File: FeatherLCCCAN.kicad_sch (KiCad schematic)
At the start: 1 part

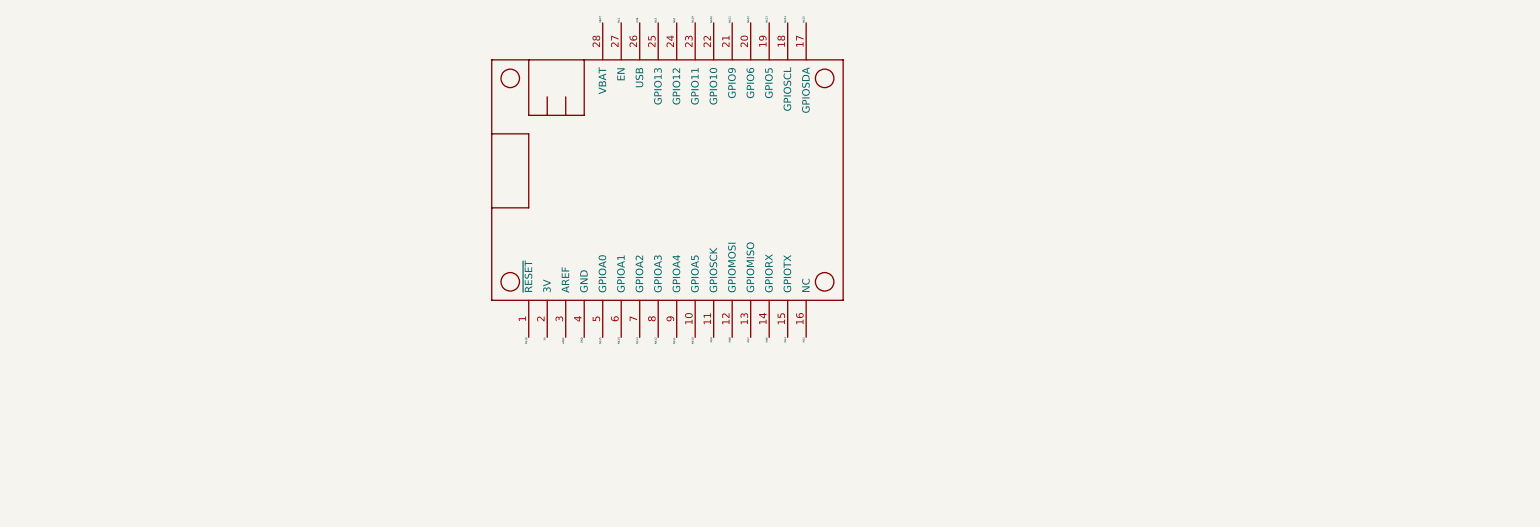
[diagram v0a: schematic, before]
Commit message: Completed LCC CAN Feather Wing.
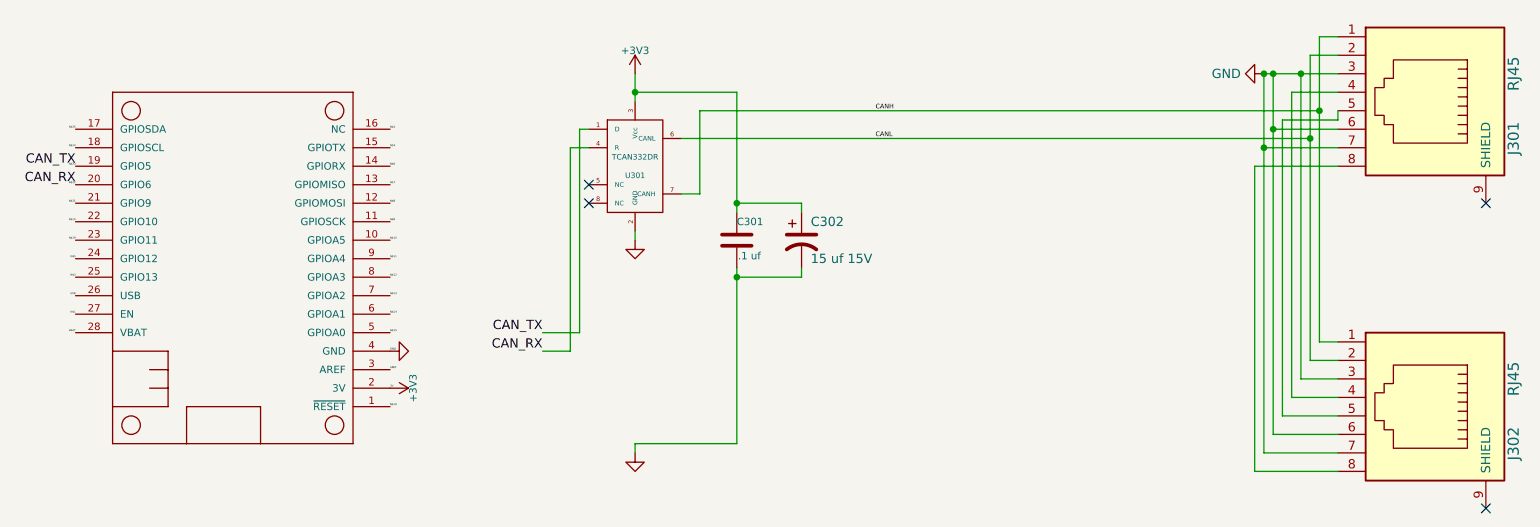
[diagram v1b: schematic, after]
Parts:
- added C301: .1 uf, Capacitor_SMD:C_0603_1608Metric, symbol ESP32-Mini32-OctalBuffer-rescue:C
- added C302: 15 uf 15V, Capacitor_SMD:CP_Elec_4x5.7, symbol ESP32-Mini32-OctalBuffer-rescue:CP1
- added J301, J302: RJ45, RJ45:RJ45_8N-S, symbol ESP32-Mini32-OctalBuffer-rescue:RJ45
- added U301: TCAN332DR, Package_SO:SOIC-8_3.9x4.9mm_P1.27mm, symbol sn65hvd233-ht:TCAN332DR
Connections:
- net GND: now also C301.2, C302.2, J301.3, J301.6, J301.7, J302.3, J302.6, J302.7, U301.2 (GND)
- net 3V renamed +3V3
- net +3V3: now also C301.1, C302.1, U301.3 (Vcc)
- net N$22 renamed CAN_RX
- net CAN_RX: now also U301.4 (R)
- net N$23 renamed CAN_TX
- net CAN_TX: now also U301.1 (D)
- new net: J301.4, J302.4
- new net: J301.5, J302.5
- new net: J301.8, J302.8
- new net CANH: J301.1, J302.1, U301.7 (CANH)
- new net CANL: J301.2, J302.2, U301.6 (CANL)
- no-connect marks 0 -> 4

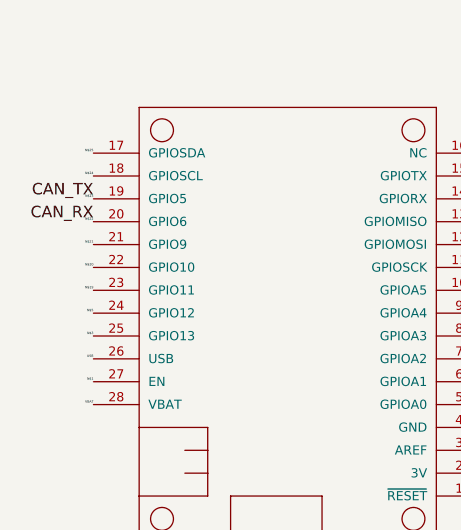
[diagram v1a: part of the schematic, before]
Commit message: Change CAN pins (allow for Adafruit 3.5" FeatherWing TFT & TouchScreen).
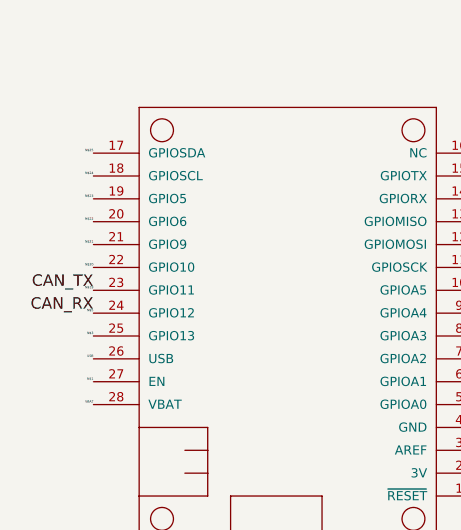
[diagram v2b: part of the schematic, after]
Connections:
- net N$19 is gone; now on net CAN_TX: MS1.23 (GPIO11)
- net N$5 is gone; now on net CAN_RX: MS1.24 (GPIO12)
- net CAN_RX: no longer MS1.20 (GPIO6)
- net CAN_TX: no longer MS1.19 (GPIO5)
- new net N$22: MS1.20 (GPIO6)
- new net N$23: MS1.19 (GPIO5)
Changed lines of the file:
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@@
     (effects (font (size 0.254 0.254)) (justify right bottom))
   )
-  (label "CAN_RX" (at 27.305 88.9 180)
+  (label "CAN_RX" (at 27.305 99.06 180)
     (effects (font (size 1.27 1.27)) (justify right bottom))
   )
@@
     (effects (font (size 0.254 0.254)) (justify left bottom))
   )
-  (label "CAN_TX" (at 27.305 86.36 180)
+  (label "CAN_TX" (at 27.305 96.52 180)
     (effects (font (size 1.27 1.27)) (justify right bottom))
   )
@@
   (symbol (lib_id "power:GND") (at 190.5 73.66 270) (unit 1)
     (in_bom yes) (on_board yes) (fields_autoplaced)
-    (property "Reference" "#PWR?" (id 0) (at 184.15 73.66 0)
+    (property "Reference" "#PWR0103" (id 0) (at 184.15 73.66 0)
       (effects (font (size 1.27 1.27)) hide)
     )
@@
     )
     (path "/2a2c9386-3deb-4c72-8b07-aa94c90312bf"
-      (reference "#PWR?") (unit 1) (value "GND") (footprint "")
+      (reference "#PWR0103") (unit 1) (value "GND") (footprint "")
     )
     (path "/00000000-0000-0000-0000-0000632c80f9"

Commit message: Update part numbers.
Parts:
- C301: LCSC (none) -> C696360; MPN (none) -> KEMET C0603C104M4RAC7411
- C302: LCSC (none) -> C2163057; MPN (none) -> Nichicon UUD1C150MCL1GS
- J301, J302, MS1: now left out of the parts list
- U301: LCSC (none) -> C73651; MPN (none) -> TCAN332DR
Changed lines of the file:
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@@
       (effects (font (size 1.524 1.524)) hide)
+    )
+    (property "LCSC" "C73651" (id 5) (at 104.14 86.36 0)
+      (effects (font (size 1.27 1.27)) hide)
+    )
+    (property "MPN" "TCAN332DR" (id 6) (at 104.14 86.36 0)
+      (effects (font (size 1.27 1.27)) hide)
     )
     (pin "1")
@@
       (effects (font (size 1.524 1.524)) hide)
     )
+    (property "LCSC" "C696360" (id 5) (at 118.11 96.52 0)
+      (effects (font (size 1.27 1.27)) hide)
+    )
+    (property "MPN" "KEMET C0603C104M4RAC7411" (id 6) (at 118.11 96.52 0)
+      (effects (font (size 1.27 1.27)) hide)
+    )
     (pin "1")
     (pin "2")
@@
       (effects (font (size 1.524 1.524)) hide)
     )
+    (property "LCSC" "C2163057" (id 5) (at 127 96.52 0)
+      (effects (font (size 1.27 1.27)) hide)
+    )
+    (property "MPN" "Nichicon UUD1C150MCL1GS" (id 6) (at 127 96.52 0)
+      (effects (font (size 1.27 1.27)) hide)
+    )
     (pin "1")
     (pin "2")
   )
   (symbol (lib_id "ESP32-Mini32-OctalBuffer-rescue:RJ45") (at 212.09 119.38 270) (unit 1)
-    (in_bom yes) (on_board yes)
+    (in_bom no) (on_board yes)
     (property "Reference" "J302" (id 0) (at 224.79 124.46 0)
       (effects (font (size 1.524 1.524)))
@@
   )
   (symbol (lib_id "ESP32-Mini32-OctalBuffer-rescue:RJ45") (at 212.09 77.47 270) (unit 1)
-    (in_bom yes) (on_board yes)
+    (in_bom no) (on_board yes)
     (property "Reference" "J301" (id 0) (at 224.79 82.55 0)
       (effects (font (size 1.524 1.524)))
@@
   )
   (symbol (lib_id "FeatherWing:FEATHERWING") (at 65.405 124.46 90) (unit 1)
-    (in_bom yes) (on_board yes)
+    (in_bom no) (on_board yes)
     (property "Reference" "MS1" (id 0) (at 65.659 124.714 0)
       (effects (font (size 1.651 1.651)) (justify left top) hide)

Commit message: Add MPN property (for PCBWay plugin).
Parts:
- U301: MPN TCAN332DR -> Texas Instruments TCAN332DR
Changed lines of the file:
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@@
       (effects (font (size 1.27 1.27)) hide)
     )
-    (property "MPN" "TCAN332DR" (id 6) (at 104.14 86.36 0)
+    (property "MPN" "Texas Instruments TCAN332DR" (id 6) (at 104.14 86.36 0)
       (effects (font (size 1.27 1.27)) hide)
     )
